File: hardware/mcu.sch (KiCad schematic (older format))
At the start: 24 parts

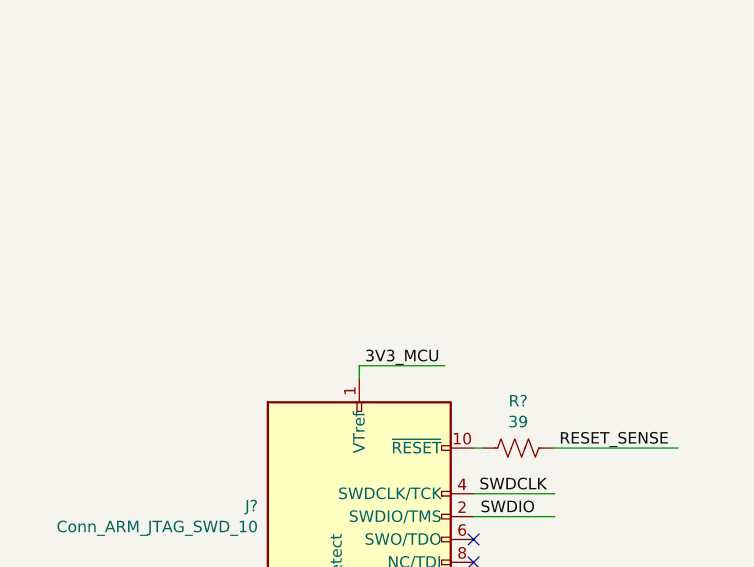
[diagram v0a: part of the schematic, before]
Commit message: hardware: add selection resistors for VTref
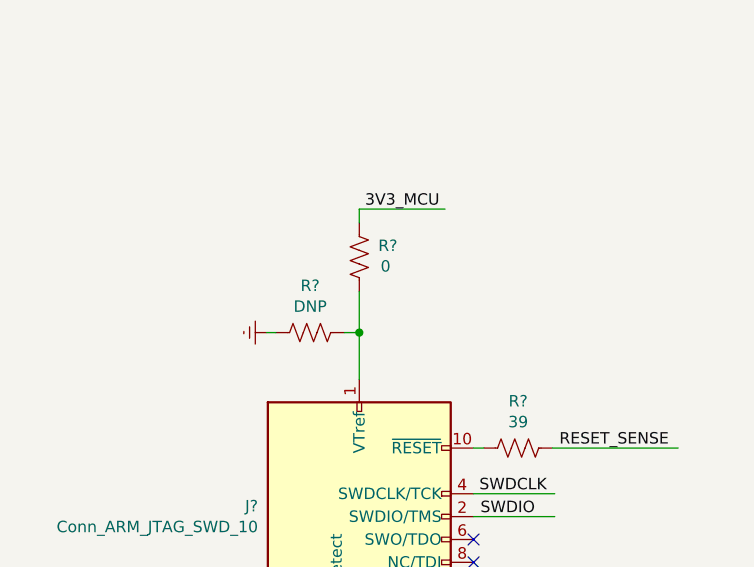
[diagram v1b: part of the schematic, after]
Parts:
- added R?: 0, symbol Device:R_US
- added R?: DNP, symbol Device:R_US
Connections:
- wire segments 81 -> 85
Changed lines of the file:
@@
 $Descr A3 16535 11693
 encoding utf-8
-Sheet 6 6
+Sheet 5 6
 Title ""
 Date ""
@@
 	2665 9850 2715 9850
 Wire Wire Line
-	2715 8575 2715 8515
-Wire Wire Line
-	2715 8515 3090 8515
-Text Label 2740 8515 0    50   ~ 0
+	2715 7890 2715 7830
+Wire Wire Line
+	2715 7830 3090 7830
+Text Label 2740 7830 0    50   ~ 0
 3V3_MCU
 Wire Wire Line
@@
 Text Notes 2525 4830 0    50   ~ 0
 Serial console
+$Comp
+L Device:R_US R?
+U 1 1 60AFCB5D
+P 2500 8370
+F 0 "R?" V 2295 8370 50  0000 C CNN
+F 1 "DNP" V 2386 8370 50  0000 C CNN
+F 2 "" V 2540 8360 50  0001 C CNN
+F 3 "~" H 2500 8370 50  0001 C CNN
+	1    2500 8370
+	0    1    1    0
+$EndComp
+$Comp
+L power:GNDREF #PWR?
+U 1 1 60AFE569
+P 2310 8370
+F 0 "#PWR?" H 2310 8120 50  0001 C CNN
+F 1 "GNDREF" H 2315 8197 50  0001 C CNN
+F 2 "" H 2310 8370 50  0001 C CNN
+F 3 "" H 2310 8370 50  0001 C CNN
+	1    2310 8370
+	0    1    1    0
+$EndComp
+Wire Wire Line
+	2310 8370 2350 8370
+Wire Wire Line
+	2715 8190 2715 8370
+Wire Wire Line
+	2650 8370 2715 8370
+Connection ~ 2715 8370
+Wire Wire Line
+	2715 8370 2715 8575
+$Comp
+L Device:R_US R?
+U 1 1 60AF25B2
+P 2715 8040
+F 0 "R?" H 2590 7990 50  0000 C CNN
+F 1 "0" H 2600 8080 50  0000 C CNN
+F 2 "" V 2755 8030 50  0001 C CNN
+F 3 "~" H 2715 8040 50  0001 C CNN
+	1    2715 8040
+	-1   0    0    1
+$EndComp
 $EndSCHEMATC

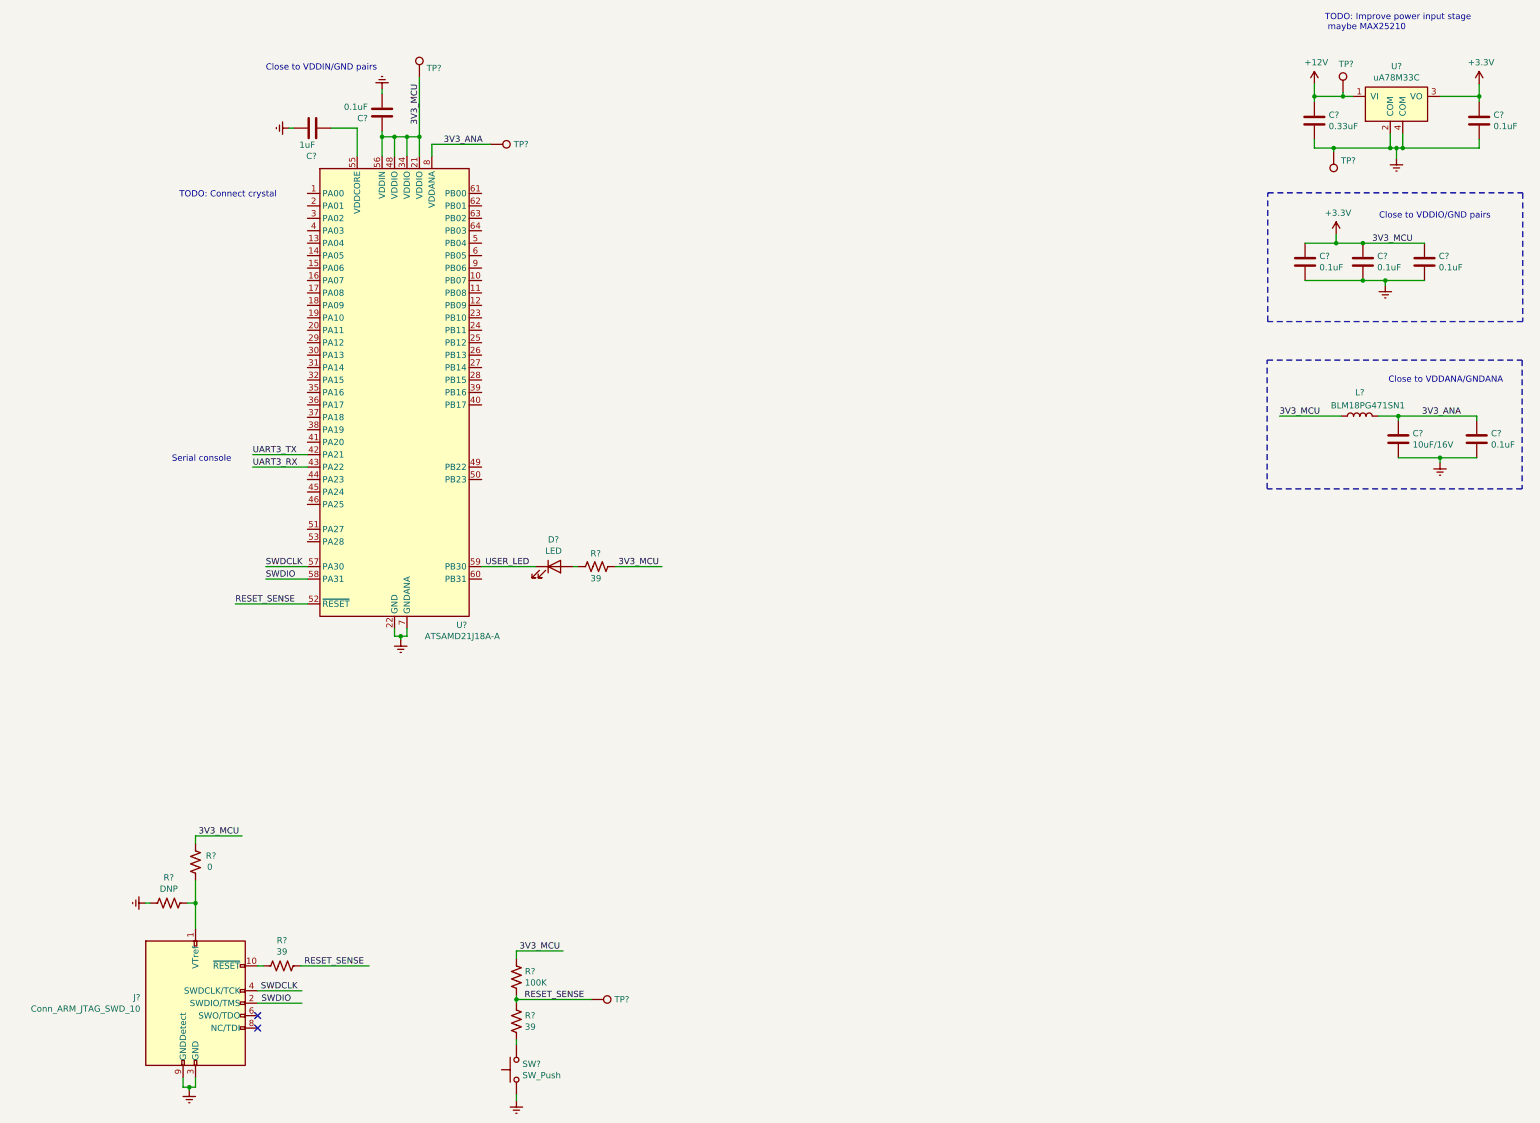
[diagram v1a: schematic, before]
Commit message: hardware: use built-in power symbols for 3V3 MCU domains
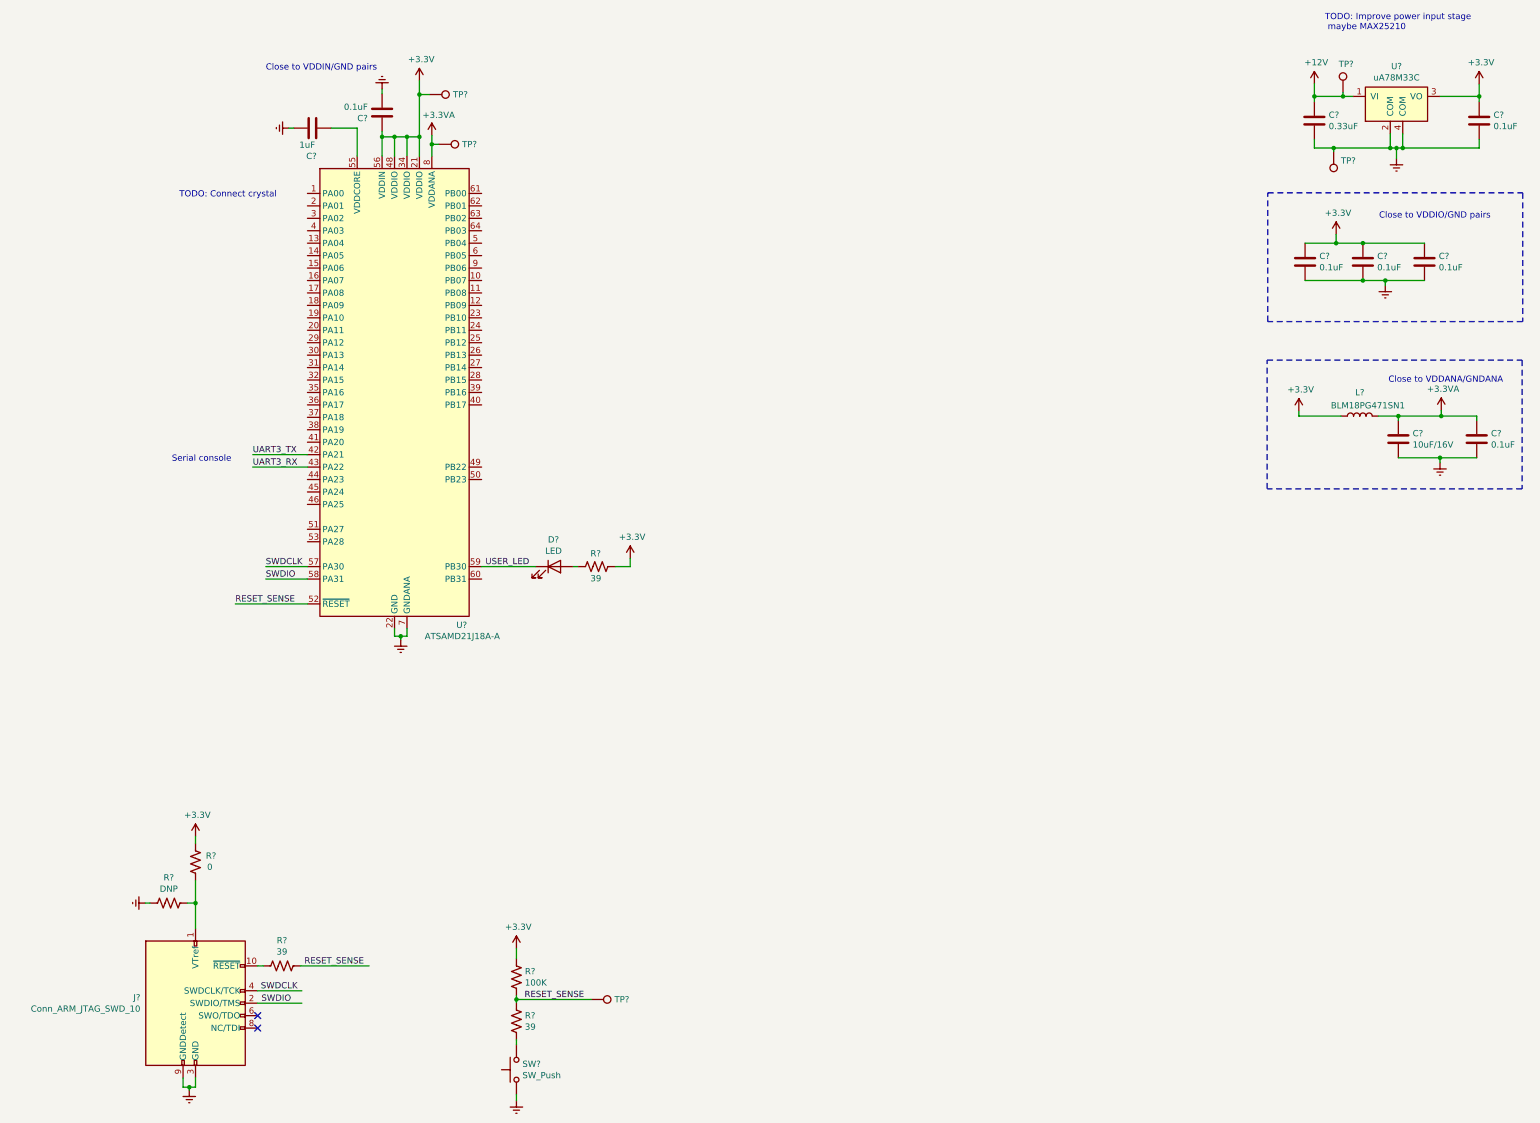
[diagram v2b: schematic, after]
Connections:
- net labels added: +3.3VA
- net labels removed: 3V3_ANA, 3V3_MCU
- wire segments 85 -> 90
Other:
- moved on the sheet: TP?
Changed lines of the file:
@@
 Wire Wire Line
 	11885 3065 12100 3065
-Text Label 12175 3065 0    50   ~ 0
-3V3_MCU
 $Comp
 L MCU_Microchip_SAMD:ATSAMD21J18A-A U?
@@
 	11330 5040 11330 4005
 Wire Wire Line
-	4515 2365 4515 2210
-Text Label 4515 2110 1    50   ~ 0
-3V3_MCU
-Wire Wire Line
 	4215 2365 4215 2210
 Wire Wire Line
 	4215 2210 4315 2210
-Connection ~ 4515 2210
-Wire Wire Line
-	4515 2210 4515 1730
 Wire Wire Line
 	4315 2365 4315 2210
@@
 Connection ~ 12385 4455
 Wire Wire Line
-	12385 4455 13015 4455
+	12385 4455 12730 4455
 $Comp
 L power:GNDREF #PWR?
@@
 Wire Wire Line
 	12720 4790 12385 4790
-Wire Wire Line
-	11430 4455 11925 4455
-Text Label 11430 4455 0    50   ~ 0
-3V3_MCU
-Text Label 12575 4455 0    50   ~ 0
-3V3_ANA
-Wire Wire Line
-	4615 2365 4615 2270
-Wire Wire Line
-	4615 2270 5085 2270
-Text Label 4710 2270 0    50   ~ 0
-3V3_ANA
 Text Notes 12305 4195 0    50   ~ 0
 Close to VDDANA/GNDANA
@@
 Wire Wire Line
 	5295 9145 5895 9145
-Wire Wire Line
-	5295 8815 5295 8755
-Wire Wire Line
-	5295 8755 5670 8755
-Text Label 5320 8755 0    50   ~ 0
-3V3_MCU
 $Comp
 L Connector:TestPoint TP?
@@
 L Connector:TestPoint TP?
 U 1 1 6086FEEE
-P 5085 2270
-F 0 "TP?" V 5085 2458 50  0000 L CNN
-F 1 "TestPoint" V 5130 2458 50  0001 L CNN
-F 2 "" H 5285 2270 50  0001 C CNN
-F 3 "~" H 5285 2270 50  0001 C CNN
-	1    5085 2270
+P 4670 2270
+F 0 "TP?" V 4670 2458 50  0000 L CNN
+F 1 "TestPoint" V 4715 2458 50  0001 L CNN
+F 2 "" H 4870 2270 50  0001 C CNN
+F 3 "~" H 4870 2270 50  0001 C CNN
+	1    4670 2270
 	0    1    1    0
 $EndComp
@@
 L Connector:TestPoint TP?
 U 1 1 6087235A
-P 4515 1730
-F 0 "TP?" H 4573 1802 50  0000 L CNN
-F 1 "TestPoint" V 4560 1918 50  0001 L CNN
-F 2 "" H 4715 1730 50  0001 C CNN
-F 3 "~" H 4715 1730 50  0001 C CNN
-	1    4515 1730
-	1    0    0    -1
+P 4595 1870
+F 0 "TP?" V 4595 2060 50  0000 L CNN
+F 1 "TestPoint" V 4640 2058 50  0001 L CNN
+F 2 "" H 4795 1870 50  0001 C CNN
+F 3 "~" H 4795 1870 50  0001 C CNN
+	1    4595 1870
+	0    1    1    0
 $EndComp
 $Comp
@@
 	2665 9850 2715 9850
 Wire Wire Line
-	2715 7890 2715 7830
-Wire Wire Line
-	2715 7830 3090 7830
-Text Label 2740 7830 0    50   ~ 0
-3V3_MCU
-Wire Wire Line
 	3215 9075 3570 9075
 Wire Wire Line
@@
 Text Notes 2585 2705 0    50   ~ 0
 TODO: Connect crystal
-Wire Wire Line
-	6090 5665 6465 5665
-Text Label 6115 5665 0    50   ~ 0
-3V3_MCU
 $Comp
 L Device:R_US R?
@@
 	-1   0    0    1
 $EndComp
+$Comp
+L power:+3.3VA #PWR?
+U 1 1 6085FCDF
+P 12730 4410
+F 0 "#PWR?" H 12730 4260 50  0001 C CNN
+F 1 "+3.3VA" H 12745 4583 50  0000 C CNN
+F 2 "" H 12730 4410 50  0001 C CNN
+F 3 "" H 12730 4410 50  0001 C CNN
+	1    12730 4410
+	1    0    0    -1
+$EndComp
+Wire Wire Line
+	12730 4455 12730 4410
+Connection ~ 12730 4455
+Wire Wire Line
+	12730 4455 13015 4455
+$Comp
+L power:+3.3V #PWR?
+U 1 1 60866AC7
+P 11585 4415
+F 0 "#PWR?" H 11585 4265 50  0001 C CNN
+F 1 "+3.3V" H 11600 4588 50  0000 C CNN
+F 2 "" H 11585 4415 50  0001 C CNN
+F 3 "" H 11585 4415 50  0001 C CNN
+	1    11585 4415
+	1    0    0    -1
+$EndComp
+Wire Wire Line
+	11585 4415 11585 4455
+Wire Wire Line
+	11585 4455 11925 4455
+$Comp
+L power:+3.3V #PWR?
+U 1 1 6086C2AA
+P 6210 5600
+F 0 "#PWR?" H 6210 5450 50  0001 C CNN
+F 1 "+3.3V" H 6225 5773 50  0000 C CNN
+F 2 "" H 6210 5600 50  0001 C CNN
+F 3 "" H 6210 5600 50  0001 C CNN
+	1    6210 5600
+	1    0    0    -1
+$EndComp
+Wire Wire Line
+	6090 5665 6210 5665
+Wire Wire Line
+	6210 5665 6210 5600
+$Comp
+L power:+3.3V #PWR?
+U 1 1 6087AE96
+P 4515 1760
+F 0 "#PWR?" H 4515 1610 50  0001 C CNN
+F 1 "+3.3V" H 4530 1933 50  0000 C CNN
+F 2 "" H 4515 1760 50  0001 C CNN
+F 3 "" H 4515 1760 50  0001 C CNN
+	1    4515 1760
+	1    0    0    -1
+$EndComp
+Wire Wire Line
+	4515 2210 4515 2365
+$Comp
+L power:+3.3VA #PWR?
+U 1 1 60898862
+P 4615 2200
+F 0 "#PWR?" H 4615 2050 50  0001 C CNN
+F 1 "+3.3VA" H 4670 2365 50  0000 C CNN
+F 2 "" H 4615 2200 50  0001 C CNN
+F 3 "" H 4615 2200 50  0001 C CNN
+	1    4615 2200
+	1    0    0    -1
+$EndComp
+Wire Wire Line
+	4615 2200 4615 2270
+Wire Wire Line
+	4670 2270 4615 2270
+Connection ~ 4615 2270
+Wire Wire Line
+	4615 2270 4615 2365
+Wire Wire Line
+	4515 2210 4515 1870
+Connection ~ 4515 2210
+Wire Wire Line
+	4515 1870 4595 1870
+Wire Wire Line
+	4515 1760 4515 1870
+Connection ~ 4515 1870
+$Comp
+L power:+3.3V #PWR?
+U 1 1 608C3B03
+P 5295 8735
+F 0 "#PWR?" H 5295 8585 50  0001 C CNN
+F 1 "+3.3V" H 5310 8908 50  0000 C CNN
+F 2 "" H 5295 8735 50  0001 C CNN
+F 3 "" H 5295 8735 50  0001 C CNN
+	1    5295 8735
+	1    0    0    -1
+$EndComp
+Wire Wire Line
+	5295 8815 5295 8735
+$Comp
+L power:+3.3V #PWR?
+U 1 1 608CDB53
+P 2715 7835
+F 0 "#PWR?" H 2715 7685 50  0001 C CNN
+F 1 "+3.3V" H 2730 8008 50  0000 C CNN
+F 2 "" H 2715 7835 50  0001 C CNN
+F 3 "" H 2715 7835 50  0001 C CNN
+	1    2715 7835
+	1    0    0    -1
+$EndComp
+Wire Wire Line
+	2715 7835 2715 7890
 $EndSCHEMATC
